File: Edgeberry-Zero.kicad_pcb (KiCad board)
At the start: 2 copper layers, 100 x 90 mm, 53 parts, among them J1 Molex_KK_1x02_P2.54mm, J2 Raspberry_Pi_2_3, J3 Edgeberry Cartridge Connector, P1 12Vin, Q1 BC547, Q2 BC547, Q3 BC547, SW1 SW_PUSH, U1 24LC256, U2 LM2596S-5.0

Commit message: Even smaller
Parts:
- G*** (x5): moved to B.Cu
- moved G*** 91.4 mm to (129.2, 68.4), turned to 90 degrees
- moved G*** 85.4 mm to (129.2, 74.6), turned to 90 degrees
- moved G*** 80.5 mm to (129.0, 80.4), turned to 90 degrees
- moved G*** 75.0 mm to (129.6, 86.8), turned to 90 degrees
- moved G*** 50.9 mm to (159.1, 160.3), turned to 180 degrees
- moved REF** 48.1 mm to (117.6, 131.3)
- moved LS1 37.5 mm to (146.0, 63.5)
- moved G*** 19.4 mm to (154.1, 77.3)
- moved Q3 7.92 mm to (135.2, 86.8)
- moved Q2 7.92 mm to (129.7, 86.8)
- moved R5 7.92 mm to (135.1, 82.5)
- moved R6 7.92 mm to (129.6, 82.5)
- moved D1 7.68 mm to (136.6, 72.8)
- moved SW1 7.68 mm to (130.3, 62.4)
- moved G*** 7.60 mm to (148.8, 135.8)
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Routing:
- net +5V: track 2.00 -> 0.00 mm
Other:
- board size 100 x 90 mm -> 92.5 x 90 mm

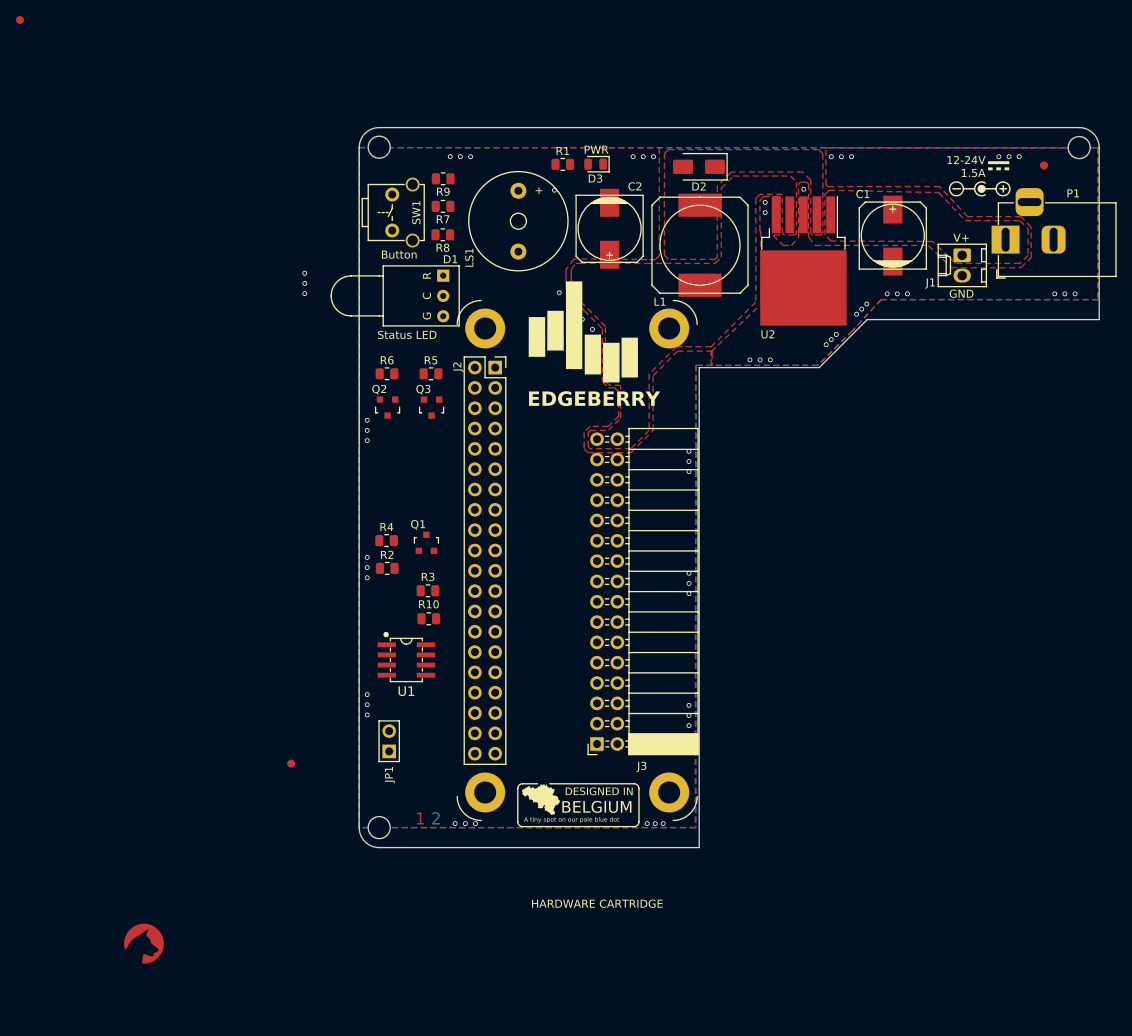
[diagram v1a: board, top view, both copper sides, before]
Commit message: Component arrangement + Mechanical dimensions
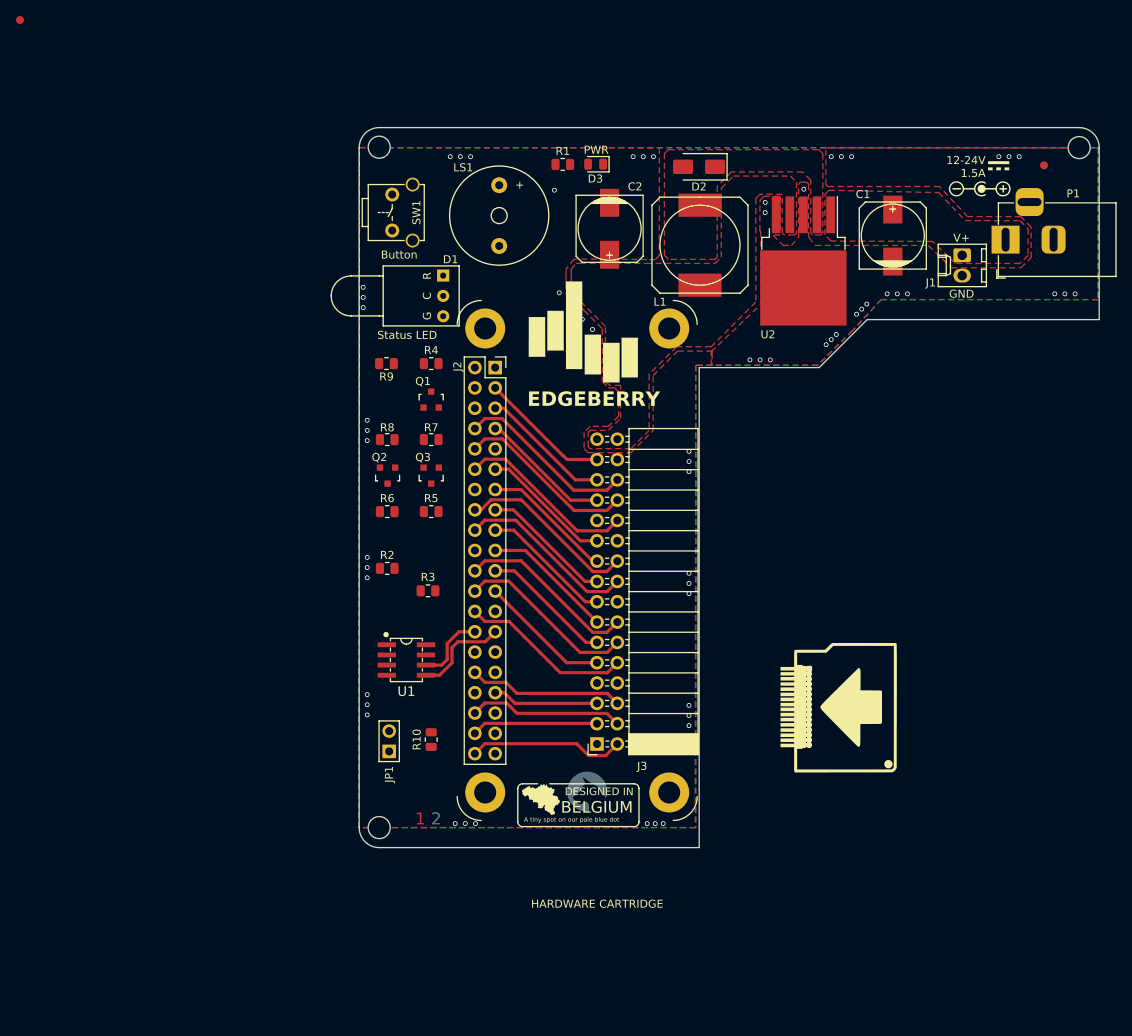
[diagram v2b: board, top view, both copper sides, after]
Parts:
- removed the REF** at (117.6, 131.3)
- G***: moved to F.Cu
- G***: moved to B.Cu
- moved G*** 58.6 mm to (154.6, 134.8), turned to 180 degrees
- moved G*** 45.0 mm to (186.1, 124.3), turned to 0 degrees
- moved R7 29.2 mm to (135.1, 90.8)
- moved R8 26.5 mm to (129.6, 90.8)
- moved R9 24.2 mm to (129.6, 81.3)
- moved R4 22.8 mm to (135.1, 81.3)
- moved Q1 17.9 mm to (135.1, 85.8)
- moved R5 17.2 mm to (135.1, 99.8)
- moved R6 17.2 mm to (129.6, 99.8)
- moved R10 15.1 mm to (135.1, 128.3), turned to 90 degrees
- moved Q3 8.50 mm to (135.1, 95.3)
- moved Q2 8.50 mm to (129.7, 95.3)
- moved LS1 2.50 mm to (143.6, 62.8)
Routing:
- net UART_RX: track 0.00 -> 22.6 mm
- net GPIO_25: track 0.00 -> 22.6 mm
- net UART_TX: track 0.00 -> 22.6 mm
- net GPIO_18: track 0.00 -> 22.6 mm
- net GPIO_23: track 0.00 -> 22.6 mm
- net GPIO_24: track 0.00 -> 22.5 mm
- net SPI_CS0: track 0.00 -> 22.5 mm
- net SPI_CS1: track 0.00 -> 21.5 mm
- net GPIO_21: track 0.00 -> 19.5 mm
- net GPIO_12: track 0.00 -> 19.4 mm
- net GPIO_16: track 0.00 -> 19.4 mm
- net SPI_SCLK: track 0.00 -> 16.4 mm
- net SPI_MISO: track 0.00 -> 16.4 mm
- net I2C_SCL: track 0.00 -> 16.4 mm
- net GPIO_27: track 0.00 -> 16.4 mm
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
